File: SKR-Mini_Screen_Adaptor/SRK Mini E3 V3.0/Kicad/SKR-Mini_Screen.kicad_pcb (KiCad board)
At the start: 2 copper layers, 22.9 x 43.2 mm, 6 parts, among them J1 Board_EXP1, J2 Board_SPI, J3 Screen_EXP1, J4 Screen_EXP2

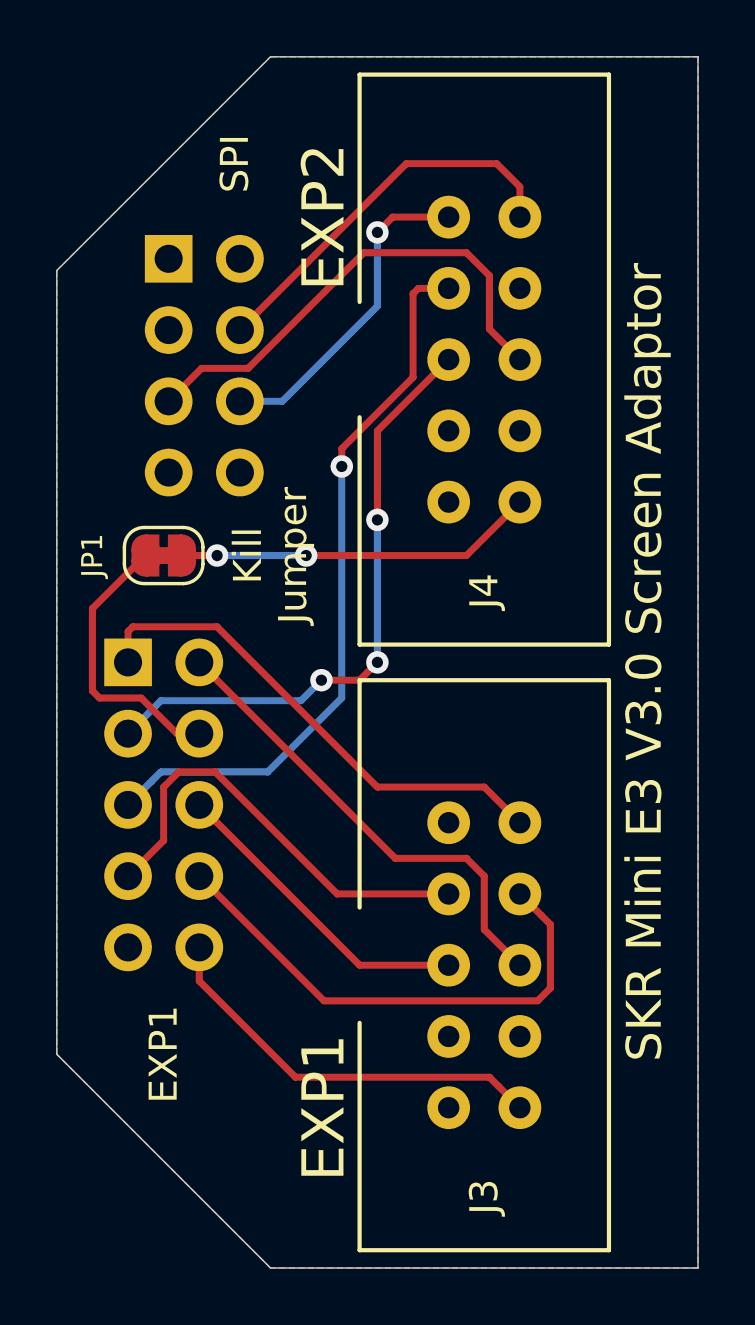
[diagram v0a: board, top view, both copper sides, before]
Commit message: V3 Cleanup and release Candidate
Update to rev B that just opens the header holes SLIGHTY for some connectors
Updates files to KiCad 6
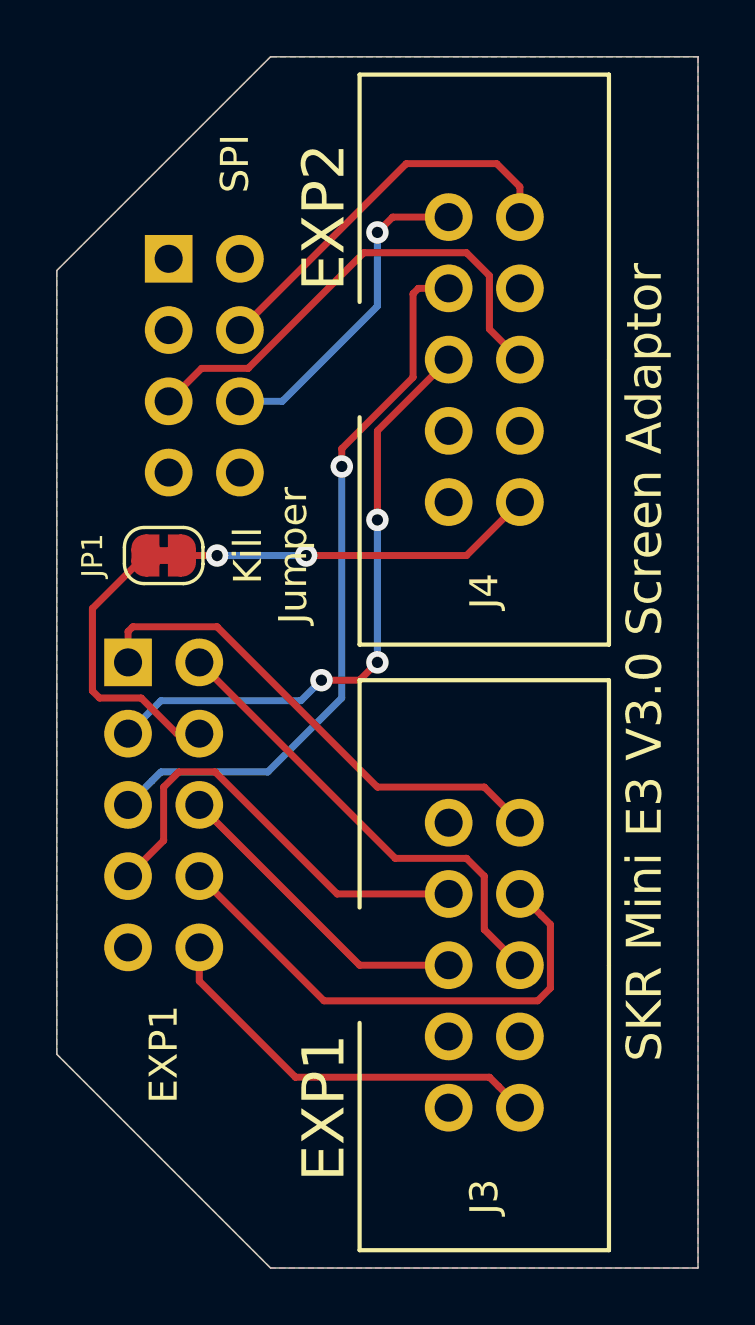
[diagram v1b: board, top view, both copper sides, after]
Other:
- board text added: "T. Abraham Rev:B"
- board text removed: "T. Abraham RevA"
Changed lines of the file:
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@@
       (effects (font (size 1 1) (thickness 0.15)))
     )
-    (fp_line (start -10.16 4.445) (end -10.16 -4.445) (layer "F.SilkS") (width 0.15))
+    (fp_line (start 10.16 -4.445) (end 10.16 4.445) (layer "F.SilkS") (width 0.15))
     (fp_line (start -2.055 4.445) (end -10.16 4.445) (layer "F.SilkS") (width 0.15))
+    (fp_line (start 0 -4.445) (end -10.16 -4.445) (layer "F.SilkS") (width 0.15))
     (fp_line (start 10.16 4.445) (end 2.055 4.445) (layer "F.SilkS") (width 0.15))
     (fp_line (start 0 -4.445) (end 10.16 -4.445) (layer "F.SilkS") (width 0.15))
-    (fp_line (start 10.16 -4.445) (end 10.16 4.445) (layer "F.SilkS") (width 0.15))
-    (fp_line (start 0 -4.445) (end -10.16 -4.445) (layer "F.SilkS") (width 0.15))
-    (pad "1" thru_hole circle (at -5.08 1.27 270) (size 1.524 1.524) (drill 0.762) (layers *.Cu *.Mask)
+    (fp_line (start -10.16 4.445) (end -10.16 -4.445) (layer "F.SilkS") (width 0.15))
+    (pad "1" thru_hole circle (at -5.08 1.27 270) (size 1.7 1.7) (drill 1) (layers *.Cu *.Mask)
       (net 19 "/Beep") (pinfunction "Pin_1") (pintype "passive"))
-    (pad "2" thru_hole circle (at -5.08 -1.27 270) (size 1.524 1.524) (drill 0.762) (layers *.Cu *.Mask)
+    (pad "2" thru_hole circle (at -5.08 -1.27 270) (size 1.7 1.7) (drill 1) (layers *.Cu *.Mask)
       (net 10 "/PB5") (pinfunction "Pin_2") (pintype "passive"))
-    (pad "3" thru_hole circle (at -2.54 1.27 270) (size 1.524 1.524) (drill 0.762) (layers *.Cu *.Mask)
+    (pad "3" thru_hole circle (at -2.54 1.27 270) (size 1.7 1.7) (drill 1) (layers *.Cu *.Mask)
       (net 4 "/PB8") (pinfunction "Pin_3") (pintype "passive"))
-    (pad "4" thru_hole circle (at -2.54 -1.27 270) (size 1.524 1.524) (drill 0.762) (layers *.Cu *.Mask)
+    (pad "4" thru_hole circle (at -2.54 -1.27 270) (size 1.7 1.7) (drill 1) (layers *.Cu *.Mask)
       (net 3 "/PB15") (pinfunction "Pin_4") (pintype "passive"))
-    (pad "5" thru_hole circle (at 0 1.27 270) (size 1.524 1.524) (drill 0.762) (layers *.Cu *.Mask)
+    (pad "5" thru_hole circle (at 0 1.27 270) (size 1.7 1.7) (drill 1) (layers *.Cu *.Mask)
       (net 5 "/PB9") (pinfunction "Pin_5") (pintype "passive"))
-    (pad "6" thru_hole circle (at 0 -1.27 270) (size 1.524 1.524) (drill 0.762) (layers *.Cu *.Mask)
+    (pad "6" thru_hole circle (at 0 -1.27 270) (size 1.7 1.7) (drill 1) (layers *.Cu *.Mask)
       (net 9 "/PA15") (pinfunction "Pin_6") (pintype "passive"))
-    (pad "7" thru_hole circle (at 2.54 1.27 270) (size 1.524 1.524) (drill 0.762) (layers *.Cu *.Mask)
+    (pad "7" thru_hole circle (at 2.54 1.27 270) (size 1.7 1.7) (drill 1) (layers *.Cu *.Mask)
       (net 18 "unconnected-(J3-Pad7)") (pinfunction "Pin_7") (pintype "passive"))
-    (pad "8" thru_hole circle (at 2.54 -1.27 270) (size 1.524 1.524) (drill 0.762) (layers *.Cu *.Mask)
+    (pad "8" thru_hole circle (at 2.54 -1.27 270) (size 1.7 1.7) (drill 1) (layers *.Cu *.Mask)
       (net 17 "unconnected-(J3-Pad8)") (pinfunction "Pin_8") (pintype "passive"))
-    (pad "9" thru_hole circle (at 5.08 1.27 270) (size 1.524 1.524) (drill 0.762) (layers *.Cu *.Mask)
+    (pad "9" thru_hole circle (at 5.08 1.27 270) (size 1.7 1.7) (drill 1) (layers *.Cu *.Mask)
       (net 2 "/GND") (pinfunction "Pin_9") (pintype "passive"))
-    (pad "10" thru_hole circle (at 5.08 -1.27 270) (size 1.524 1.524) (drill 0.762) (layers *.Cu *.Mask)
+    (pad "10" thru_hole circle (at 5.08 -1.27 270) (size 1.7 1.7) (drill 1) (layers *.Cu *.Mask)
       (net 1 "/+5V") (pinfunction "Pin_10") (pintype "passive"))
     (model "${KIPRJMOD}/3D_Models/702461001.stp"
@@
       (effects (font (size 1 1) (thickness 0.15)))
     )
+    (fp_line (start 0 -4.445) (end -10.16 -4.445) (layer "F.SilkS") (width 0.15))
     (fp_line (start 0 -4.445) (end 10.16 -4.445) (layer "F.SilkS") (width 0.15))
-    (fp_line (start 0 -4.445) (end -10.16 -4.445) (layer "F.SilkS") (width 0.15))
+    (fp_line (start -2.055 4.445) (end -10.16 4.445) (layer "F.SilkS") (width 0.15))
     (fp_line (start 10.16 4.445) (end 2.055 4.445) (layer "F.SilkS") (width 0.15))
     (fp_line (start 10.16 -4.445) (end 10.16 4.445) (layer "F.SilkS") (width 0.15))
     (fp_line (start -10.16 4.445) (end -10.16 -4.445) (layer "F.SilkS") (width 0.15))
-    (fp_line (start -2.055 4.445) (end -10.16 4.445) (layer "F.SilkS") (width 0.15))
-    (pad "1" thru_hole circle (at -5.08 1.27 270) (size 1.524 1.524) (drill 0.762) (layers *.Cu *.Mask)
+    (pad "1" thru_hole circle (at -5.08 1.27 270) (size 1.7 1.7) (drill 1) (layers *.Cu *.Mask)
       (net 13 "/MISO") (pinfunction "Pin_1") (pintype "passive"))
-    (pad "2" thru_hole circle (at -5.08 -1.27 270) (size 1.524 1.524) (drill 0.762) (layers *.Cu *.Mask)
+    (pad "2" thru_hole circle (at -5.08 -1.27 270) (size 1.7 1.7) (drill 1) (layers *.Cu *.Mask)
       (net 12 "/SCK") (pinfunction "Pin_2") (pintype "passive"))
-    (pad "3" thru_hole circle (at -2.54 1.27 270) (size 1.524 1.524) (drill 0.762) (layers *.Cu *.Mask)
+    (pad "3" thru_hole circle (at -2.54 1.27 270) (size 1.7 1.7) (drill 1) (layers *.Cu *.Mask)
       (net 6 "/PA10") (pinfunction "Pin_3") (pintype "passive"))
-    (pad "4" thru_hole circle (at -2.54 -1.27 270) (size 1.524 1.524) (drill 0.762) (layers *.Cu *.Mask)
+    (pad "4" thru_hole circle (at -2.54 -1.27 270) (size 1.7 1.7) (drill 1) (layers *.Cu *.Mask)
       (net 22 "unconnected-(J4-Pad4)") (pinfunction "Pin_4") (pintype "passive"))
-    (pad "5" thru_hole circle (at 0 1.27 270) (size 1.524 1.524) (drill 0.762) (layers *.Cu *.Mask)
+    (pad "5" thru_hole circle (at 0 1.27 270) (size 1.7 1.7) (drill 1) (layers *.Cu *.Mask)
       (net 8 "/PA9") (pinfunction "Pin_5") (pintype "passive"))
-    (pad "6" thru_hole circle (at 0 -1.27 270) (size 1.524 1.524) (drill 0.762) (layers *.Cu *.Mask)
+    (pad "6" thru_hole circle (at 0 -1.27 270) (size 1.7 1.7) (drill 1) (layers *.Cu *.Mask)
       (net 11 "/MOSI") (pinfunction "Pin_6") (pintype "passive"))
-    (pad "7" thru_hole circle (at 2.54 1.27 270) (size 1.524 1.524) (drill 0.762) (layers *.Cu *.Mask)
+    (pad "7" thru_hole circle (at 2.54 1.27 270) (size 1.7 1.7) (drill 1) (layers *.Cu *.Mask)
       (net 21 "unconnected-(J4-Pad7)") (pinfunction "Pin_7") (pintype "passive"))
-    (pad "8" thru_hole circle (at 2.54 -1.27 270) (size 1.524 1.524) (drill 0.762) (layers *.Cu *.Mask)
+    (pad "8" thru_hole circle (at 2.54 -1.27 270) (size 1.7 1.7) (drill 1) (layers *.Cu *.Mask)
       (net 20 "unconnected-(J4-Pad8)") (pinfunction "Pin_8") (pintype "passive"))
-    (pad "9" thru_hole circle (at 5.08 1.27 270) (size 1.524 1.524) (drill 0.762) (layers *.Cu *.Mask)
+    (pad "9" thru_hole circle (at 5.08 1.27 270) (size 1.7 1.7) (drill 1) (layers *.Cu *.Mask)
       (net 2 "/GND") (pinfunction "Pin_9") (pintype "passive"))
-    (pad "10" thru_hole circle (at 5.08 -1.27 270) (size 1.524 1.524) (drill 0.762) (layers *.Cu *.Mask)
+    (pad "10" thru_hole circle (at 5.08 -1.27 270) (size 1.7 1.7) (drill 1) (layers *.Cu *.Mask)
       (net 14 "/Kill") (pinfunction "Pin_10") (pintype "passive"))
     (model "${KIPRJMOD}/3D_Models/702461001.stp"
@@
     (effects (font (size 1 1) (thickness 0.2)) (justify mirror))
   )
-  (gr_text "T. Abraham RevA" (at 132.715 106.68 90) (layer "B.SilkS")
+  (gr_text "T. Abraham Rev:B" (at 132.715 106.68 90) (layer "B.SilkS")
     (effects (font (size 1 1) (thickness 0.2)) (justify mirror))
   )
